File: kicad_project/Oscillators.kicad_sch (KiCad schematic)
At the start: 10 parts, among them U20 74LVC1G80, X1 24.000MHz

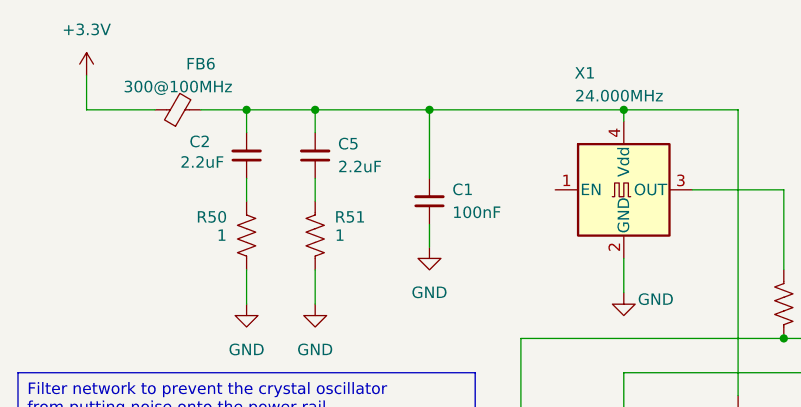
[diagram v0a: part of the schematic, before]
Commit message: Finish new SD card schematic, ERC passing!
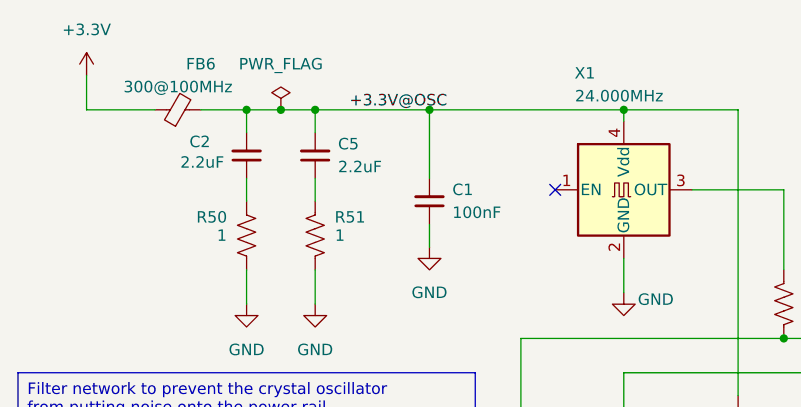
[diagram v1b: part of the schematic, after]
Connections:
- net +3.3V@OSC: now reaches C1.2, C2.2, C5.2, FB6.2, U20.5 (VCC), X1.4 (Vdd)
- no-connect marks 0 -> 1
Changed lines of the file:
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@@
+	)
+	(junction
+		(at 74.93 92.71)
+		(diameter 0)
+		(color 0 0 0 0)
 	)
 	(junction
@@
 		(color 0 0 0 0)
 	)
+	(no_connect
+		(at 105.41 101.6)
+	)
 	(wire
 		(pts
@@
 	(wire
 		(pts
-			(xy 71.12 92.71) (xy 78.74 92.71)
+			(xy 71.12 92.71) (xy 74.93 92.71)
 		)
 		(stroke
@@
 		(pts
 			(xy 66.04 92.71) (xy 71.12 92.71)
+		)
+		(stroke
+			(width 0)
+			(type default)
+		)
+	)
+	(wire
+		(pts
+			(xy 74.93 92.71) (xy 78.74 92.71)
 		)
 		(stroke
@@
 			)
 			(justify left top)
+		)
+	)
+	(label "+3.3V@OSC"
+		(at 82.55 92.71 0)
+		(effects
+			(font
+				(size 1.27 1.27)
+			)
+			(justify left bottom)
 		)
 	)
@@
 					(unit 1)
 				)
+			)
+		)
+	)
+	(symbol
+		(lib_id "power:PWR_FLAG")
+		(at 74.93 92.71 0)
+		(unit 1)
+		(exclude_from_sim no)
+		(in_bom yes)
+		(on_board yes)
+		(dnp no)
+		(fields_autoplaced yes)
+		(property "Reference" "#FLG02"
+			(at 74.93 90.805 0)
+			(effects
+				(font
+					(size 1.27 1.27)
+				)
+				(hide yes)
+			)
+		)
+		(property "Value" "PWR_FLAG"
+			(at 74.93 87.63 0)
+			(effects
+				(font
+					(size 1.27 1.27)
+				)
+			)
+		)
+		(property "Footprint" ""
+			(at 74.93 92.71 0)
+			(effects
+				(font
+					(size 1.27 1.27)
+				)
+				(hide yes)
+			)
+		)
+		(property "Datasheet" "~"
+			(at 74.93 92.71 0)
+			(effects
+				(font
+					(size 1.27 1.27)
+				)
+				(hide yes)
+			)
+		)
+		(property "Description" "Special symbol for telling ERC where power comes from"
+			(at 74.93 92.71 0)
+			(effects
+				(font
+					(size 1.27 1.27)
+				)
+				(hide yes)
+			)
+		)
+		(pin "1"
+		)
+		(instances
+			(project "mbed-ce-ci-shield-v2"
+				(path "/a0f40274-9469-4bcf-885c-e8b8a490ea54/afb13bad-f815-4420-a8e2-616c627fc38e"
+					(reference "#FLG02")
+					(unit 1)
+				)

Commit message: Fix some BOM isues
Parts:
- R50, R51: LibRef P1.0RCT-ND -> ERJ-8RQF1R0V; SKU P120FCT-ND -> P1.0RCT-ND
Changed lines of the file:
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@@
 			)
 		)
-		(property "LibRef" "P1.0RCT-ND"
+		(property "LibRef" "ERJ-8RQF1R0V"
 			(at 71.12 106.68 0)
 			(effects
@@
 			)
 		)
-		(property "SKU" "P120FCT-ND"
+		(property "SKU" "P1.0RCT-ND"
 			(at 71.12 106.68 0)
 			(effects
@@
 			)
 		)
-		(property "LibRef" "P1.0RCT-ND"
-			(at 78.74 106.68 0)
-			(effects
-				(font
-					(size 1.27 1.27)
-				)
-				(hide yes)
-			)
-		)
-		(property "SKU" "P120FCT-ND"
-			(at 78.74 106.68 0)
-			(effects
+		(property "LibRef" "ERJ-8RQF1R0V"
+			(at 78.74 106.68 0)
+			(effects
+				(font
+					(size 1.27 1.27)
+				)
+				(hide yes)
+			)
+		)
+		(property "SKU" "P1.0RCT-ND"
+			(at 78.74 106.68 0)
+			(effects

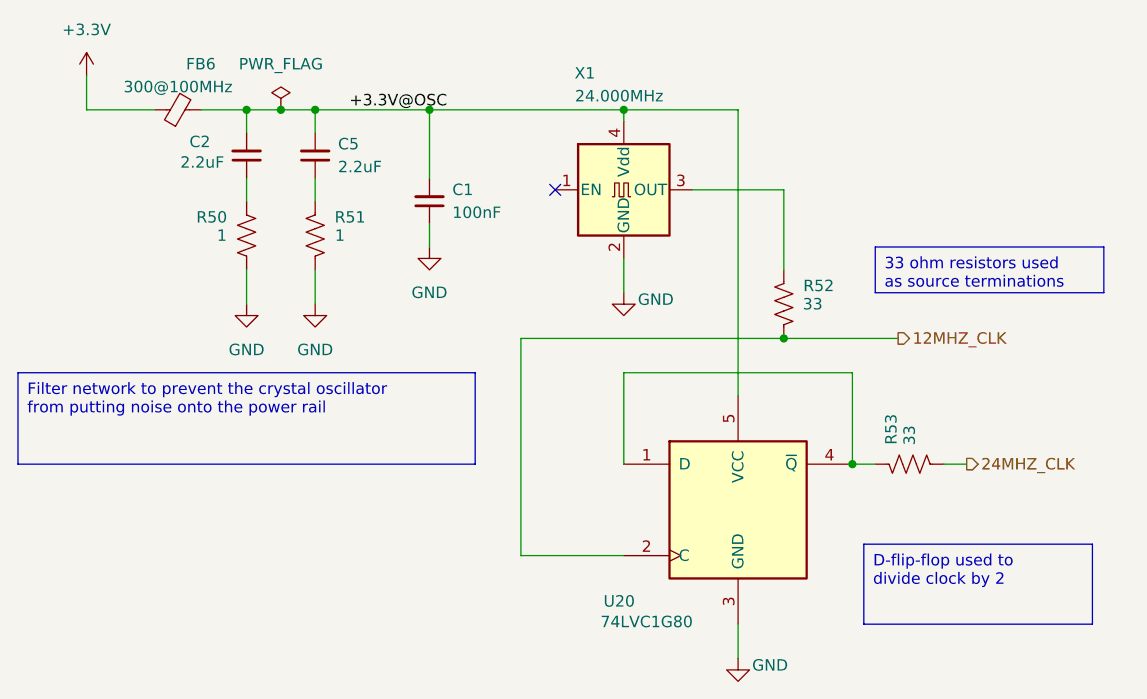
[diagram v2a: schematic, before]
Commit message: Switch out multiplexer, start switch FX2LP out for RP2040
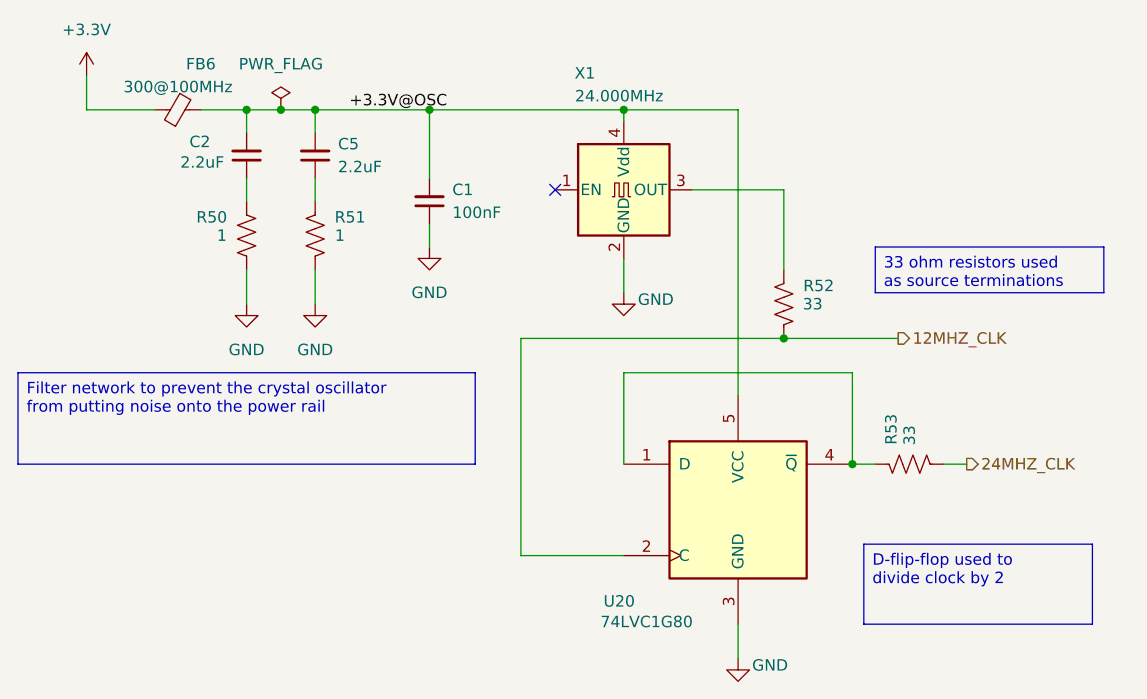
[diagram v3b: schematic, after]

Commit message: Start on Rev 4, switch to RPi Pico
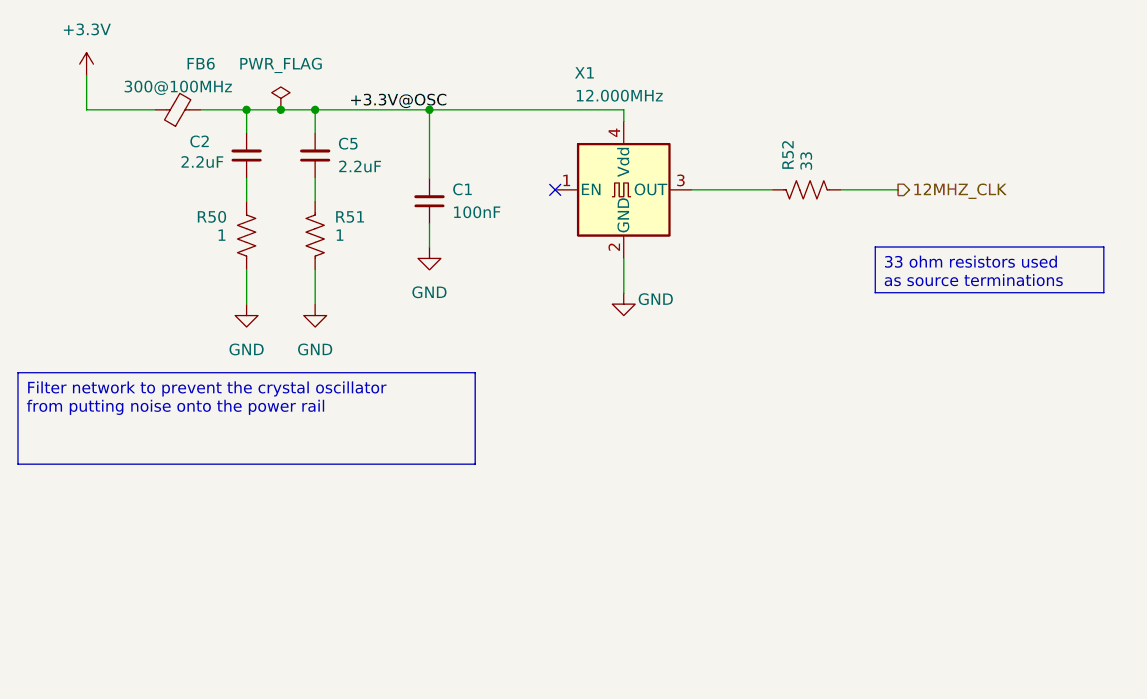
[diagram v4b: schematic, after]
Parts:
- removed R53: 33, Resistor_SMD:R_1206_3216Metric, symbol Device:R_US
- removed U20: 74LVC1G80, Package_TO_SOT_SMD:SOT-23-5, symbol 74xGxx:74LVC1G80
- X1: value 24.000MHz -> 12.000MHz; LibRef ASV-24.000MHZ-EJ-T -> ASV-12.000MHZ-EJ-T; SKU 535-9317-1-ND -> 535-9309-1-ND
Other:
- moved on the sheet: R52
